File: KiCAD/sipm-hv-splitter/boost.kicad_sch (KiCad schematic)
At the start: 52 parts, among them Q1 BSS138, Q2 BSS138, Q3 BSS138, U2 INA201, U3 LM51581, U4 LT3014xS5, U5 AD5270

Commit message: finish BOM entries on schematic
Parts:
- R12: CatNo (none) -> 541-5389-1-ND; MfgNo (none) -> CRCW06033K16FKEAC
- R13: CatNo (none) -> P150KHCT-ND; MfgNo (none) -> ERJ-3EKF1503V
- R14: CatNo (none) -> 541-4044-1-ND; MfgNo (none) -> CRCW06032K49FKEAC
- R16, R5, R6: value 10k -> 10.0k
- R18: CatNo (none) -> RMCF0603FT510KCT-ND; MfgNo (none) -> RMCF0603FT510K
- R19: CatNo (none) -> RMCF0603FT24K0CT-ND; MfgNo (none) -> RMCF0603FT24K0
- R9: CatNo RMCF0603FT3R00CT-ND -> 4506-MFCR1206F3R00QHRCT-ND; MfgNo RMCF0603FT3R00 -> MFCR1206F3R00QHR
- U3: CatNo (none) -> 296-LM51581RTERCT-ND; MfgNo (none) -> LM51581RTER
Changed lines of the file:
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@@
 			)
 		)
-		(property "Value" "10k"
+		(property "Value" "10.0k"
 			(at 55.88 172.7199 0)
 			(effects
@@
 			)
 		)
-		(property "MfgNo" ""
+		(property "MfgNo" "RMCF0603FT24K0"
 			(at 218.44 53.34 0)
 			(effects
@@
 			)
 		)
-		(property "CatNo" ""
+		(property "CatNo" "RMCF0603FT24K0CT-ND"
 			(at 218.44 53.34 0)
 			(effects
@@
 			)
 		)
-		(property "MfgNo" ""
+		(property "MfgNo" "RMCF0603FT510K"
 			(at 218.44 45.72 0)
 			(effects
@@
 			)
 		)
-		(property "CatNo" ""
+		(property "CatNo" "RMCF0603FT510KCT-ND"
 			(at 218.44 45.72 0)
 			(effects
@@
 			)
 		)
-		(property "MfgNo" "RMCF0603FT3R00"
+		(property "MfgNo" "MFCR1206F3R00QHR"
 			(at 91.44 96.52 90)
 			(effects
@@
 			)
 		)
-		(property "CatNo" "RMCF0603FT3R00CT-ND"
+		(property "CatNo" "4506-MFCR1206F3R00QHRCT-ND"
 			(at 91.44 96.52 90)
 			(effects
@@
 			)
 		)
-		(property "Value" "10k"
+		(property "Value" "10.0k"
 			(at 124.46 45.7199 0)
 			(effects
@@
 			)
 		)
+		(property "CatNo" "296-LM51581RTERCT-ND"
+			(at 72.39 148.59 0)
+			(effects
+				(font
+					(size 1.27 1.27)
+				)
+				(hide yes)
+			)
+		)
+		(property "MfgNo" "LM51581RTER"
+			(at 72.39 148.59 0)
+			(effects
+				(font
+					(size 1.27 1.27)
+				)
+				(hide yes)
+			)
+		)
 		(pin "8"
 		)
@@
 			)
 		)
+		(property "CatNo" "541-5389-1-ND"
+			(at 102.87 173.99 0)
+			(effects
+				(font
+					(size 1.27 1.27)
+				)
+				(hide yes)
+			)
+		)
+		(property "MfgNo" "CRCW06033K16FKEAC"
+			(at 102.87 173.99 0)
+			(effects
+				(font
+					(size 1.27 1.27)
+				)
+				(hide yes)
+			)
+		)
 		(pin "1"
 		)
@@
 			)
 		)
+		(property "CatNo" "P150KHCT-ND"
+			(at 107.95 143.51 0)
+			(effects
+				(font
+					(size 1.27 1.27)
+				)
+				(hide yes)
+			)
+		)
+		(property "MfgNo" "ERJ-3EKF1503V"
+			(at 107.95 143.51 0)
+			(effects
+				(font
+					(size 1.27 1.27)
+				)
+				(hide yes)
+			)
+		)
 		(pin "1"
 		)
@@
 			)
 		)
+		(property "CatNo" "541-4044-1-ND"
+			(at 107.95 154.94 0)
+			(effects
+				(font
+					(size 1.27 1.27)
+				)
+				(hide yes)
+			)
+		)
+		(property "MfgNo" "CRCW06032K49FKEAC"
+			(at 107.95 154.94 0)
+			(effects
+				(font
+					(size 1.27 1.27)
+				)
+				(hide yes)
+			)
+		)
 		(pin "1"
 		)
@@
 			)
 		)
-		(property "Value" "10k"
+		(property "Value" "10.0k"
 			(at 52.832 43.434 0)
 			(effects

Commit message: Candidate V1.0 for review/fab
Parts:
- removed TP1: IMON, TestPoint:TestPoint_Pad_D1.0mm, symbol Connector:TestPoint
- removed TP2: VIN60, TestPoint:TestPoint_Pad_D1.0mm, symbol Connector:TestPoint
- removed TP3: CMP, TestPoint:TestPoint_Pad_D1.0mm, symbol Connector:TestPoint
- removed TP4: VR_IN, TestPoint:TestPoint_Pad_D1.0mm, symbol Connector:TestPoint
- removed TP5: VR_ADJ, TestPoint:TestPoint_Pad_D1.0mm, symbol Connector:TestPoint
- removed TP6: DPOT, TestPoint:TestPoint_Pad_D1.0mm, symbol Connector:TestPoint
- removed TP7: VSENSE, TestPoint:TestPoint_Pad_D1.0mm, symbol Connector:TestPoint

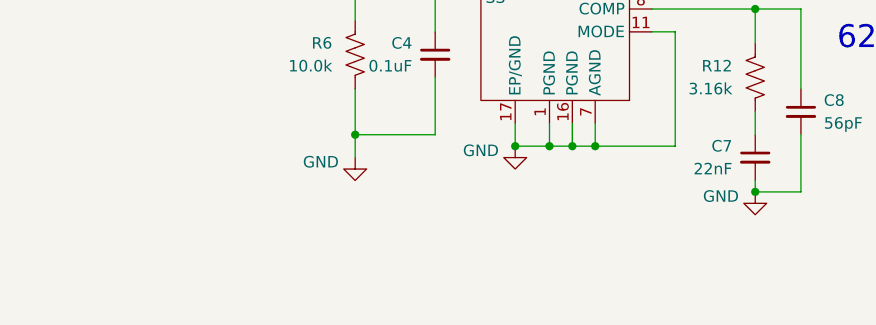
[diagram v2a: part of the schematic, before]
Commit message: add mtg holes, L2 gnd fill
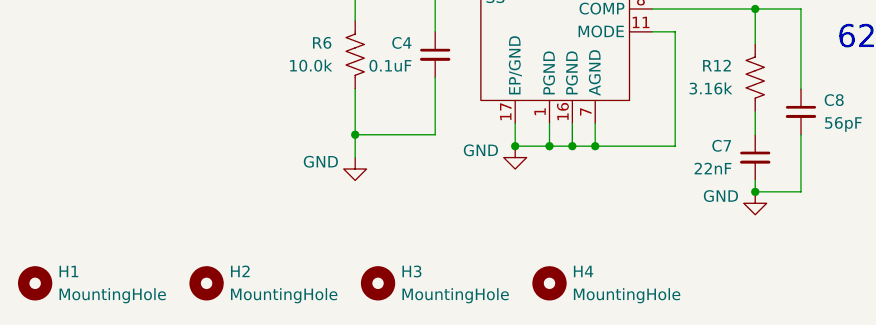
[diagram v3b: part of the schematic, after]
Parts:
- added H1, H2, H3, H4: MountingHole, MountingHole:MountingHole_2.2mm_M2, symbol Mechanical:MountingHole

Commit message: update testing
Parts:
- R13: value 150k -> 180k; CatNo P150KHCT-ND -> P180KHCT-ND; MfgNo ERJ-3EKF1503V -> (none)
- R17: value 2.50M 1% -> 2.7M 1%; CatNo RMCF0603FT2M49CT-ND -> ??; MfgNo RMCF0603FT2M49 -> (none)
- R3: value 140k -> 75k; CatNo 311-140KHRCT-ND -> 311-75KHRCT-ND; MfgNo RC0603FR-07140KL -> (none)
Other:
- note added: "140k"
- note added: "150k"
- note added: "2.5M 1%"
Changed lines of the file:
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@@
 		)
 	)
+	(text "150k"
+		(exclude_from_sim no)
+		(at 103.124 147.574 0)
+		(effects
+			(font
+				(size 1.27 1.27)
+			)
+		)
+	)
 	(text "62V BOOST CONVERTER"
 		(exclude_from_sim no)
@@
 		)
 	)
+	(text "2.5M 1%"
+		(exclude_from_sim no)
+		(at 182.626 54.864 0)
+		(effects
+			(font
+				(size 1.27 1.27)
+			)
+		)
+	)
 	(text "(optional)\nSoft start"
 		(exclude_from_sim no)
@@
 		)
 	)
+	(text "140k"
+		(exclude_from_sim no)
+		(at 29.21 62.23 0)
+		(effects
+			(font
+				(size 1.27 1.27)
+			)
+		)
+	)
 	(junction
 		(at 87.63 71.12)
@@
 		)
 	)
+	(polyline
+		(pts
+			(xy 100.33 147.32) (xy 105.41 147.32)
+		)
+		(stroke
+			(width 0)
+			(type default)
+		)
+	)
 	(wire
 		(pts
@@
 		)
 	)
+	(polyline
+		(pts
+			(xy 177.8 54.61) (xy 186.69 54.61)
+		)
+		(stroke
+			(width 0)
+			(type default)
+		)
+	)
 	(wire
 		(pts
@@
 		)
 	)
+	(polyline
+		(pts
+			(xy 25.908 61.976) (xy 32.258 61.976)
+		)
+		(stroke
+			(width 0)
+			(type default)
+		)
+	)
 	(wire
 		(pts
@@
 			)
 		)
-		(property "Value" "140k"
-			(at 34.544 60.706 0)
+		(property "Value" "75k"
+			(at 30.734 59.182 0)
 			(effects
 				(font
@@
 			)
 		)
-		(property "MfgNo" "RC0603FR-07140KL"
+		(property "MfgNo" ""
 			(at 38.1 59.69 0)
 			(effects
@@
 			)
 		)
-		(property "CatNo" "311-140KHRCT-ND"
+		(property "CatNo" "311-75KHRCT-ND"
 			(at 38.1 59.69 0)
 			(effects
@@
 			)
 		)
-		(property "Value" "2.50M 1%"
+		(property "Value" "2.7M 1%"
 			(at 177.8 50.7999 0)
 			(effects
@@
 			)
 		)
-		(property "MfgNo" "RMCF0603FT2M49"
+		(property "MfgNo" ""
 			(at 175.26 49.53 0)
 			(effects
@@
 			)
 		)
-		(property "CatNo" "RMCF0603FT2M49CT-ND"
+		(property "CatNo" "??"
 			(at 175.26 49.53 0)
 			(effects
@@
 			)
 		)
-		(property "Value" "150k"
-			(at 105.41 144.7799 0)
+		(property "Value" "180k"
+			(at 105.41 144.78 0)
 			(effects
 				(font
@@
 			)
 		)
-		(property "CatNo" "P150KHCT-ND"
+		(property "CatNo" "P180KHCT-ND"
 			(at 107.95 143.51 0)
 			(effects
@@
 			)
 		)
-		(property "MfgNo" "ERJ-3EKF1503V"
+		(property "MfgNo" ""
 			(at 107.95 143.51 0)
 			(effects
